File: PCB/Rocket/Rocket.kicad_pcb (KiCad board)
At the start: 2 copper layers, 71 x 69.5 mm, 47 parts, among them J1 Conn_01x08_Pin, J2 Conn_01x04_Pin, J3 Conn_01x07_Pin, J4 Micro_SD_Card, J5 Conn_ARM_JTAG_SWD_10, J6 Conn_01x04_Pin, J7 1987724, SW1 CK_KMS2xxG, SW2 CK_KMS2xxG, U1 STM32L476RGTx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

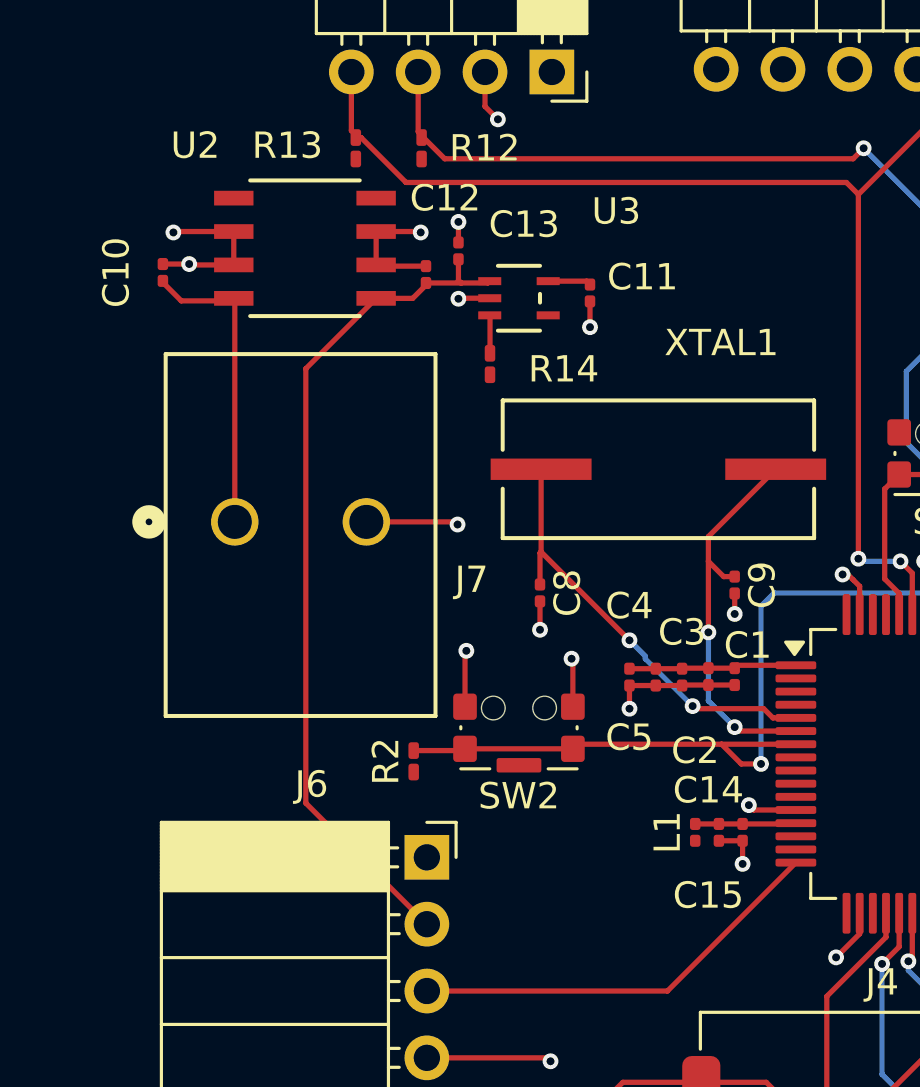
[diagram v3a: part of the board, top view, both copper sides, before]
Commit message: Adjusted trace widths.
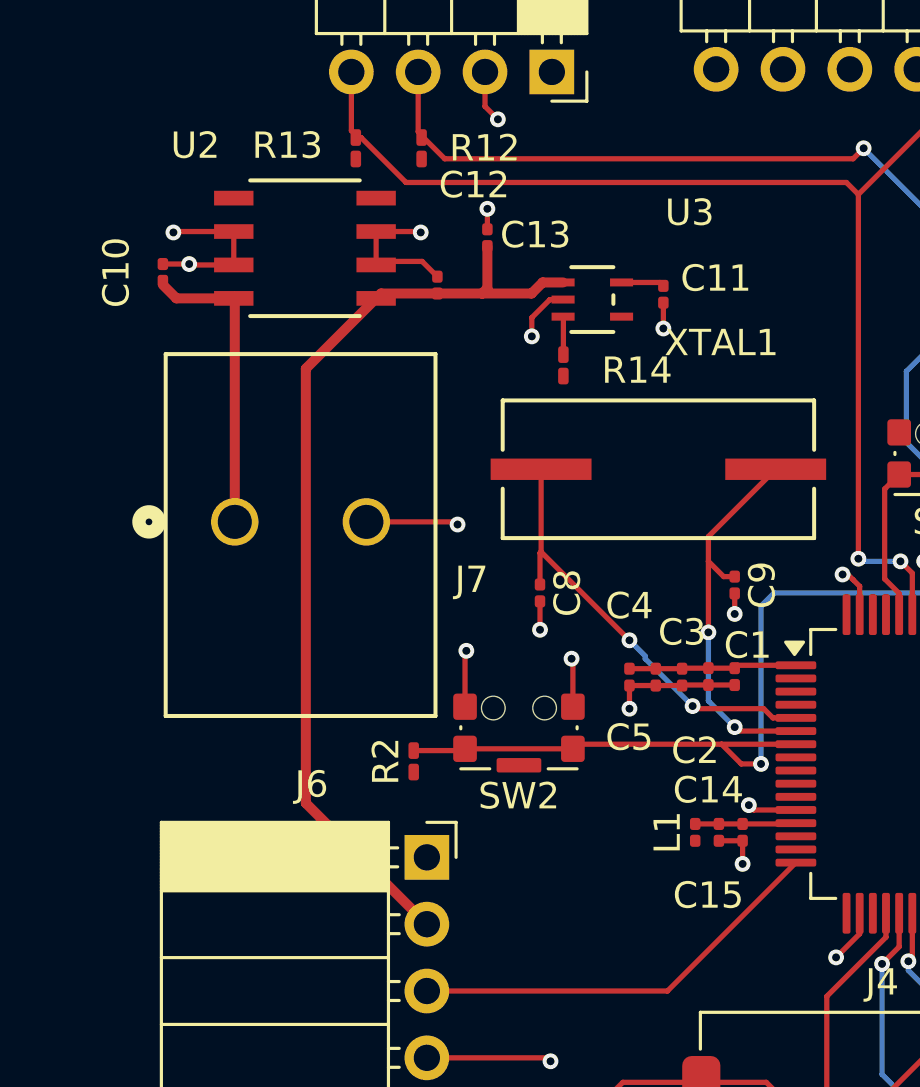
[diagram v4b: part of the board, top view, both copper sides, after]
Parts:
- moved U3 2.79 mm to (124.6, 52.8)
- moved C11 2.79 mm to (127.3, 52.6)
- moved R14 2.79 mm to (123.5, 55.3)
- moved C12 1.21 mm to (120.6, 50.5)
- moved C13 0.59 mm to (118.7, 52.3)
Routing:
- net +5V: track 32.4 -> 36.0 mm
- net GND: track 72.9 -> 74.6 mm
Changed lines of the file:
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@@
 	(footprint "Capacitor_SMD:C_0201_0603Metric"
 		(layer "F.Cu")
-		(at 118.2666 51.9 -90)
+		(at 118.7 52.3 -90)
 		(descr "Capacitor SMD 0201 (0603 Metric), square (rectangular) end terminal, IPC_7351 nominal, (Body size source: https://www.vishay.com/docs/20052/crcw0201e3.pdf), generated with kicad-footprint-generator")
 		(tags "capacitor")
@@
 	(footprint "Capacitor_SMD:C_0201_0603Metric"
 		(layer "F.Cu")
-		(at 119.5 51 90)
+		(at 120.6 50.5 90)
 		(descr "Capacitor SMD 0201 (0603 Metric), square (rectangular) end terminal, IPC_7351 nominal, (Body size source: https://www.vishay.com/docs/20052/crcw0201e3.pdf), generated with kicad-footprint-generator")
 		(tags "capacitor")
@@
 	(footprint "MIC5365-3.3YC5-TR:SC-70_C5_MCH"
 		(layer "F.Cu")
-		(at 121.8 52.8)
+		(at 124.58875 52.849999)
 		(tags "MIC5365-3.3YC5-TR ")
 		(property "Reference" "U3"
@@
 	(footprint "Capacitor_SMD:C_0201_0603Metric"
 		(layer "F.Cu")
-		(at 124.5 52.6 90)
+		(at 127.28875 52.649999 90)
 		(descr "Capacitor SMD 0201 (0603 Metric), square (rectangular) end terminal, IPC_7351 nominal, (Body size source: https://www.vishay.com/docs/20052/crcw0201e3.pdf), generated with kicad-footprint-generator")
 		(tags "capacitor")
@@
 	(footprint "Resistor_SMD:R_0201_0603Metric_Pad0.64x0.40mm_HandSolder"
 		(layer "F.Cu")
-		(at 120.7 55.3 -90)
+		(at 123.48875 55.349999 -90)
 		(descr "Resistor SMD 0201 (0603 Metric), square (rectangular) end terminal, IPC_7351 nominal with elongated pad for handsoldering. (Body size source: https://www.vishay.com/docs/20052/crcw0201e3.pdf), generated with kicad-footprint-generator")
 		(tags "resistor handsolder")
@@
 	)
 	(segment
-		(start 120.7 53.461249)
-		(end 120.68875 53.449999)
+		(start 123.48875 53.511248)
+		(end 123.4775 53.499998)
 		(width 0.2)
 		(layer "F.Cu")
@@
 	)
 	(segment
-		(start 120.7 54.8925)
-		(end 120.7 53.461249)
+		(start 123.48875 54.942499)
+		(end 123.48875 53.511248)
 		(width 0.2)
 		(layer "F.Cu")
@@
 	)
 	(segment
-		(start 122.91125 52.150001)
-		(end 124.370001 52.150001)
+		(start 125.7 52.2)
+		(end 127.158751 52.2)
 		(width 0.2)
 		(layer "F.Cu")
@@
 	)
 	(segment
-		(start 124.370001 52.150001)
-		(end 124.5 52.28)
+		(start 127.158751 52.2)
+		(end 127.28875 52.329999)
 		(width 0.2)
 		(layer "F.Cu")
@@
 	)
 	(segment
-		(start 111 61.3)
-		(end 111 52.8435)
-		(width 0.2)
+		(start 108.7806 52.805)
+		(end 108.2666 52.291)
+		(width 0.381)
 		(layer "F.Cu")
 		(net 74)
 	)
 	(segment
-		(start 108.9666 52.9)
-		(end 110.8665 52.9)
-		(width 0.2)
-		(layer "F.Cu")
-		(net 74)
-	)
-	(segment
-		(start 108.2666 52.2)
-		(end 108.9666 52.9)
-		(width 0.2)
+		(start 110.9615 52.805)
+		(end 108.7806 52.805)
+		(width 0.381)
 		(layer "F.Cu")
 		(net 74)
@@
 		(start 111 52.8435)
 		(end 110.9615 52.805)
-		(width 0.2)
-		(layer "F.Cu")
-		(net 74)
-	)
-	(segment
-		(start 110.8665 52.9)
-		(end 110.9615 52.805)
-		(width 0.2)
+		(width 0.508)
 		(layer "F.Cu")
 		(net 74)
 	)
 	(segment
-		(start 108.2666 52.14)
-		(end 108.2666 52.2)
-		(width 0.2)
+		(start 111 61.3)
+		(end 111 52.8435)
+		(width 0.381)
 		(layer "F.Cu")
 		(net 74)
 	)
 	(segment
-		(start 118.2666 52.3)
-		(end 117.7616 52.805)
-		(width 0.2)
+		(start 113.7 55.4767)
+		(end 116.3717 52.805)
+		(width 0.381)
 		(layer "F.Cu")
 		(net 75)
 	)
 	(segment
-		(start 119.5 51.32)
-		(end 119.5 52.12)
-		(width 0.2)
+		(start 116.5567 52.62)
+		(end 116.3717 52.805)
+		(width 0.381)
 		(layer "F.Cu")
 		(net 75)
 	)
 	(segment
-		(start 113.7 55.4767)
-		(end 116.3717 52.805)
-		(width 0.2)
+		(start 120.4 52.62)
+		(end 118.7 52.62)
+		(width 0.381)
 		(layer "F.Cu")
 		(net 75)
 	)
 	(segment
-		(start 118.2666 52.22)
-		(end 118.2666 52.3)
-		(width 0.2)
+		(start 123.4775 52.2)
+		(end 122.7 52.2)
+		(width 0.381)
 		(layer "F.Cu")
 		(net 75)
 	)
 	(segment
-		(start 119.5 52.12)
-		(end 119.6 52.22)
-		(width 0.2)
+		(start 113.7 71.99)
+		(end 113.7 55.4767)
+		(width 0.381)
 		(layer "F.Cu")
 		(net 75)
 	)
 	(segment
-		(start 118.2666 52.22)
-		(end 119.6 52.22)
-		(width 0.2)
+		(start 120.6 52.42)
+		(end 120.6 50.82)
+		(width 0.381)
 		(layer "F.Cu")
 		(net 75)
 	)
 	(segment
-		(start 117.7616 52.805)
-		(end 116.3717 52.805)
-		(width 0.2)
+		(start 120.4 52.62)
+		(end 120.6 52.42)
+		(width 0.381)
 		(layer "F.Cu")
 		(net 75)
 	)
 	(segment
-		(start 113.7 71.99)
-		(end 113.7 55.4767)
-		(width 0.2)
+		(start 122.7 52.2)
+		(end 122.28 52.62)
+		(width 0.381)
 		(layer "F.Cu")
 		(net 75)
 	)
 	(segment
-		(start 119.6 52.22)
-		(end 120.618751 52.22)
-		(width 0.2)
+		(start 122.28 52.62)
+		(end 120.4 52.62)
+		(width 0.381)
 		(layer "F.Cu")
 		(net 75)
@@
 		(start 118.3 76.59)
 		(end 113.7 71.99)
-		(width 0.2)
+		(width 0.381)
 		(layer "F.Cu")
 		(net 75)
 	)
 	(segment
-		(start 120.618751 52.22)
-		(end 120.68875 52.150001)
-		(width 0.2)
+		(start 118.7 52.62)
+		(end 116.5567 52.62)
+		(width 0.381)
 		(layer "F.Cu")
 		(net 75)
@@
 	)
 	(segment
-		(start 124.5 52.92)
-		(end 124.5 53.9)
+		(start 116.5067 51.4)
+		(end 116.3717 51.535)
+		(width 0.2)
+		(layer "F.Cu")
+		(net 76)
+	)
+	(segment
+		(start 127.28875 52.969999)
+		(end 127.28875 53.949999)
 		(width 0.2)
 		(layer "F.Cu")
@@
 	)
 	(segment
-		(start 119.5 52.82)
-		(end 119.52 52.8)
-		(width 0.2)
-		(layer "F.Cu")
-		(net 76)
-	)
-	(segment
 		(start 126 67.52)
 		(end 126 68.4)
@@
 	)
 	(segment
-		(start 116.4167 51.58)
-		(end 116.3717 51.535)
-		(width 0.2)
-		(layer "F.Cu")
-		(net 76)
-	)
-	(segment
 		(start 123.85 66.55)
 		(end 123.8 66.5)
@@
 	)
 	(segment
-		(start 118.2666 51.58)
-		(end 116.4167 51.58)
+		(start 137.9 83.4)
+		(end 137.8 83.3)
 		(width 0.2)
 		(layer "F.Cu")
@@
 	)
 	(segment
-		(start 137.9 83.4)
-		(end 137.8 83.3)
+		(start 122.976949 52.849999)
+		(end 123.4775 52.849999)
 		(width 0.2)
 		(layer "F.Cu")
@@
 	)
 	(segment
-		(start 119.52 52.8)
-		(end 120.68875 52.8)
-		(width 0.2)
-		(layer "F.Cu")
-		(net 76)
-	)
-	(segment
 		(start 122.6 64.32)
 		(end 122.6 65.4)
@@
 	)
 	(segment
-		(start 119.5 50.68)
-		(end 119.5 49.9)
+		(start 120.6 50.18)
+		(end 120.6 49.4)
 		(width 0.2)
 		(layer "F.Cu")
@@
 	)
 	(segment
+		(start 118.7 51.98)
+		(end 118.12 51.4)
+		(width 0.2)
+		(layer "F.Cu")
+		(net 76)
+	)
+	(segment
 		(start 133.852062 77.852062)
 		(end 134.75 76.954124)
@@
 	)
 	(segment
+		(start 122.28875 53.538198)
+		(end 122.976949 52.849999)
+		(width 0.2)
+		(layer "F.Cu")
+		(net 76)
+	)
+	(segment
 		(start 146.25 91.75)
 		(end 146.2 91.8)
@@
 	)
 	(segment
+		(start 122.28875 54.249999)
+		(end 122.28875 53.538198)
+		(width 0.2)
+		(layer "F.Cu")
+		(net 76)
+	)
+	(segment
 		(start 123.85 68.325)
 		(end 123.85 66.55)
@@
 	)
 	(segment
+		(start 118.12 51.4)
+		(end 116.5067 51.4)
+		(width 0.2)
+		(layer "F.Cu")
+		(net 76)
+	)
+	(segment
 		(start 119.75 68.325)
 		(end 119.75 66.25)
@@
 	)
 	(via
-		(at 119.5 52.82)
+		(at 122.28875 54.249999)
 		(size 0.6)
 		(drill 0.3)
@@
 	)
 	(via
-		(at 119.5 49.9)
+		(at 120.6 49.4)
 		(size 0.6)
 		(drill 0.3)
@@
 	)
 	(via
-		(at 124.5 53.9)
+		(at 127.28875 53.949999)
 		(size 0.6)
 		(drill 0.3)

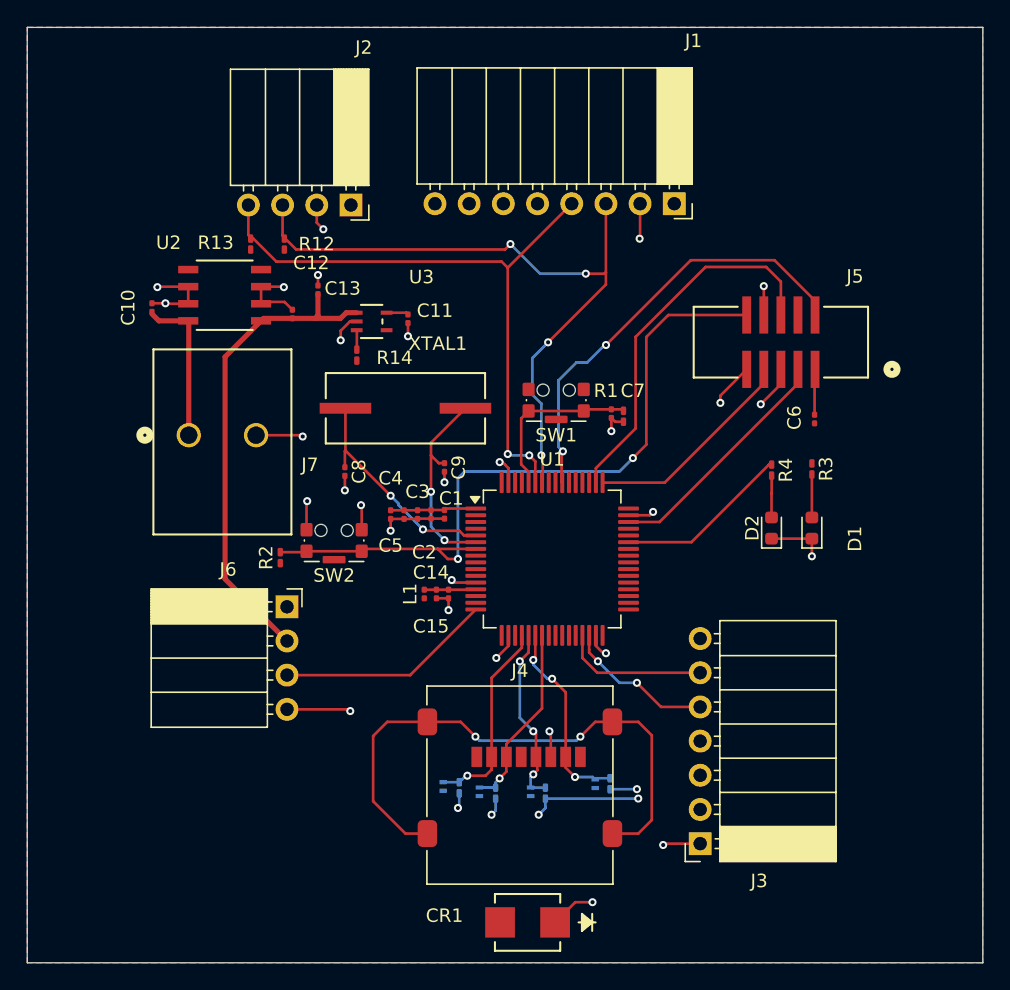
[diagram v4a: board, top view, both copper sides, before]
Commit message: Fixed I2C traces.
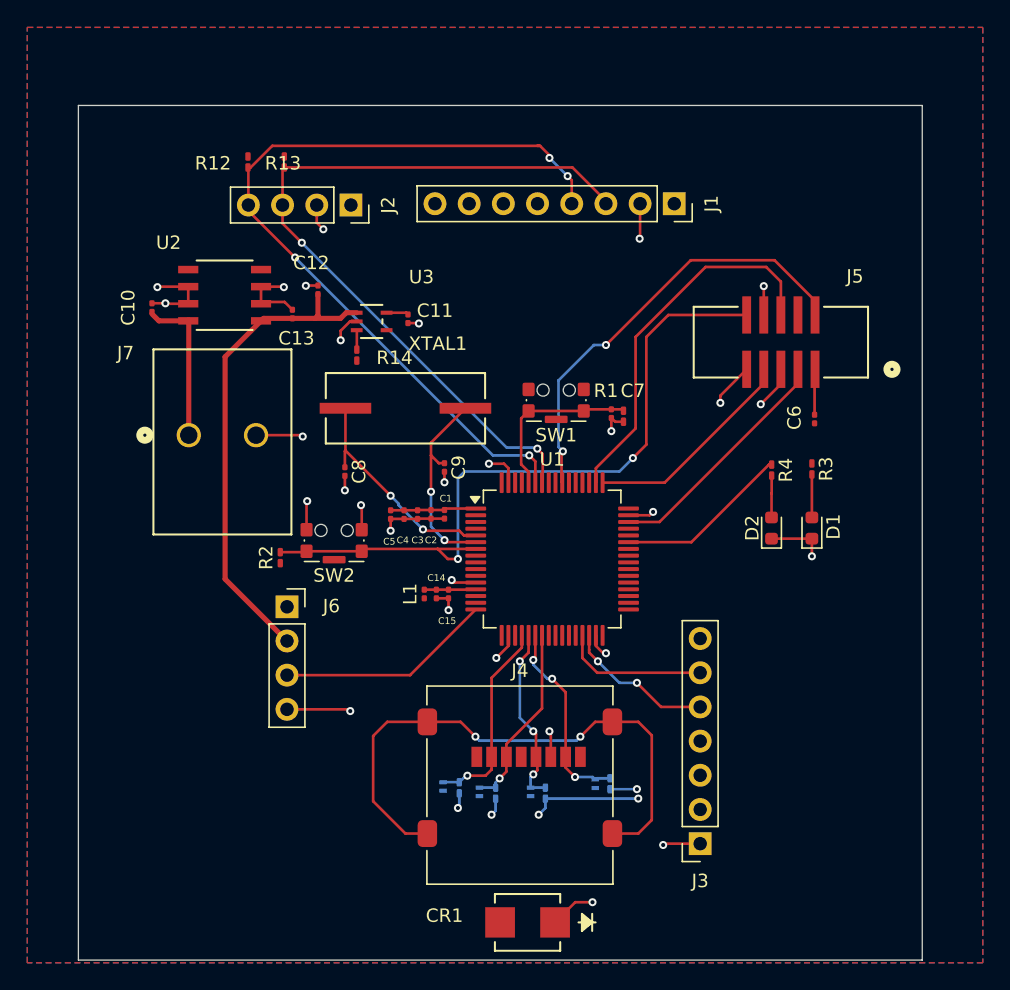
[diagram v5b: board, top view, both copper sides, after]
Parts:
- J1: footprint Connector_PinSocket_2.54mm:PinSocket_1x08_P2.54mm_Horizontal -> Connector_PinSocket_2.54mm:PinSocket_1x08_P2.54mm_Vertical
- J2, J6: footprint Connector_PinSocket_2.54mm:PinSocket_1x04_P2.54mm_Horizontal -> Connector_PinSocket_2.54mm:PinSocket_1x04_P2.54mm_Vertical
- J3: footprint Connector_PinSocket_2.54mm:PinSocket_1x07_P2.54mm_Horizontal -> Connector_PinSocket_2.54mm:PinSocket_1x07_P2.54mm_Vertical
- moved R13 6.10 mm to (115.4, 41.0), turned to 90 degrees
- moved R12 6.10 mm to (118.1, 41.0), turned to 90 degrees
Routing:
- net /SDA: track 46.9 -> 61.7 mm, vias 2 -> 4
- net /SCL: track 50.9 -> 57.7 mm, vias 4 -> 2
- net GND: track 74.6 -> 75.3 mm
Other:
- board size 71 x 69.5 mm -> 62.7 x 63.5 mm

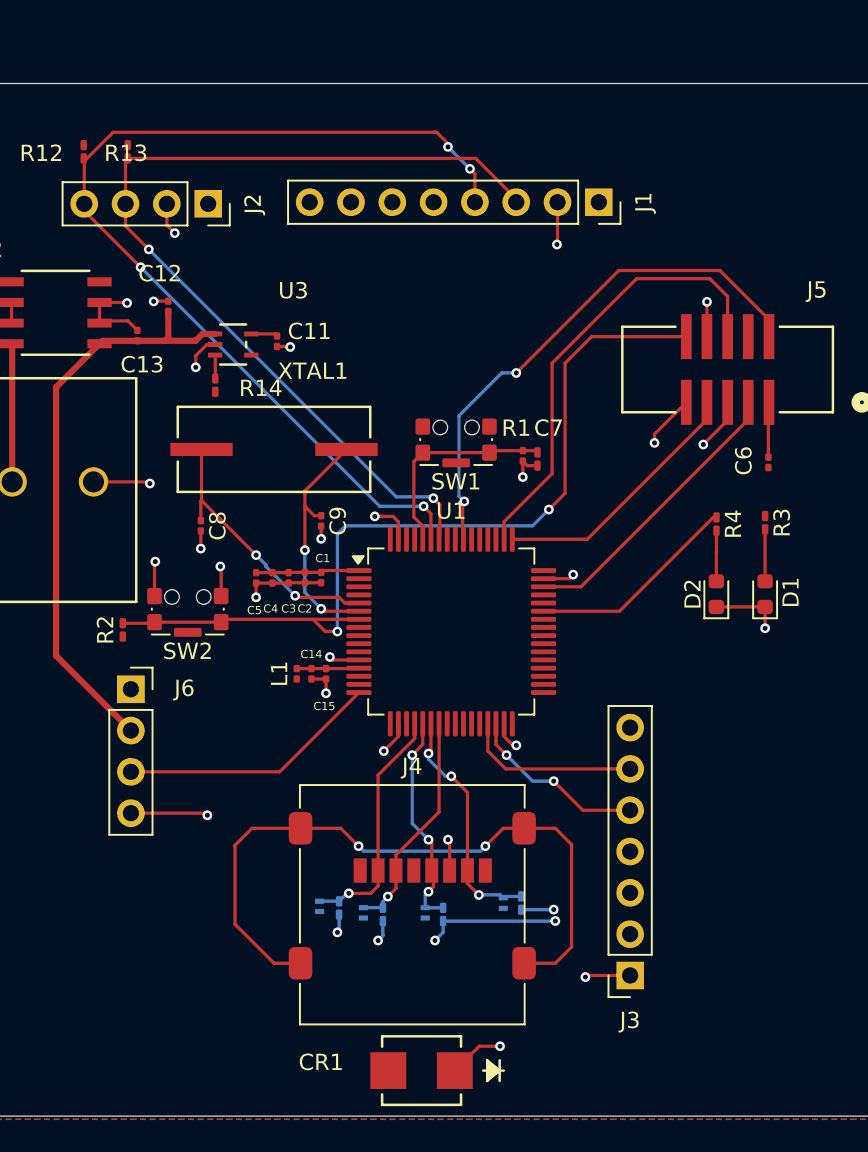
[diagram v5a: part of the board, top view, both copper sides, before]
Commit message: Fixed SPI connections.
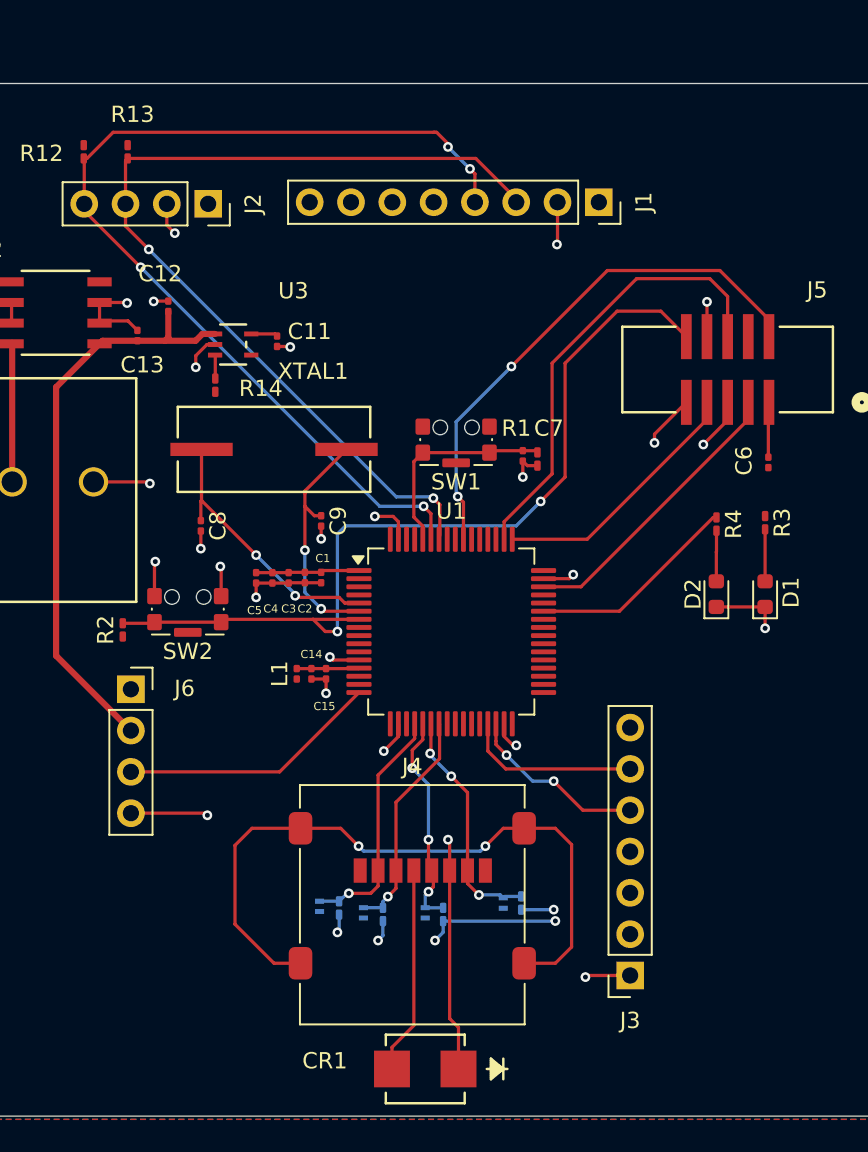
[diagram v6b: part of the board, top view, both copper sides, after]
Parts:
- moved CR1 0.25 mm to (136.4, 97.4)
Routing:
- net +3.3V: track 21.1 -> 33.8 mm
- net GND: track 75.3 -> 83.7 mm, vias 29 -> 28
- net /NRST: track 53.6 -> 54.3 mm
- net /MISO: track 14.8 -> 14.1 mm
